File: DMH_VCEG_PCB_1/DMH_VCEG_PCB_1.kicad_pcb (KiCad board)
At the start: 2 copper layers, 148 x 175 mm, 243 parts, among them J1 TS_Jack_6.35mm_Sw, J10 TS_Jack_6.35mm_Sw, J100 IDC_02x08, J11 TS_Jack_6.35mm_Sw, J12 TS_Jack_6.35mm_Sw, J13 TS_Jack_6.35mm_Sw, J14 TS_Jack_6.35mm_Sw, J15 TS_Jack_6.35mm_Sw, J16 TS_Jack_6.35mm_Sw, J17 TS_Jack_6.35mm_Sw, J18 TS_Jack_6.35mm_Sw, J19 TS_Jack_6.35mm_Sw, J2 TS_Jack_6.35mm_Sw, J20 TS_Jack_6.35mm_Sw, J200 IDC_02x08, J21 Conn_01x10_PinHeader, J22 Conn_01x10_PinHeader, J23 Conn_01x10_PinHeader, J24 Conn_01x06_PinHeader, J25 Conn_01x10_PinHeader, J26 Conn_01x10_PinHeader, J27 Conn_01x10_PinHeader, J3 TS_Jack_6.35mm_Sw, J4 TS_Jack_6.35mm_Sw, J5 TS_Jack_6.35mm_Sw, J6 TS_Jack_6.35mm_Sw, J7 TS_Jack_6.35mm_Sw, J8 TS_Jack_6.35mm_Sw, J9 TS_Jack_6.35mm_Sw, Q1 BC558, Q17 BC558, Q18 BC558, Q19 BC548, Q2 BC558, Q20 BC548, Q21 BS170, Q22 BS170, Q3 BC548, Q4 BC548, Q5 BS170, Q6 BS170, U1 TL074, U11 TL074, U12 4001, U13 40106, U15 TL074, U16 4001, U17 TL074, U2 4001, U25 4001, U3 40106, U5 TL074, U6 4001, U7 TL074

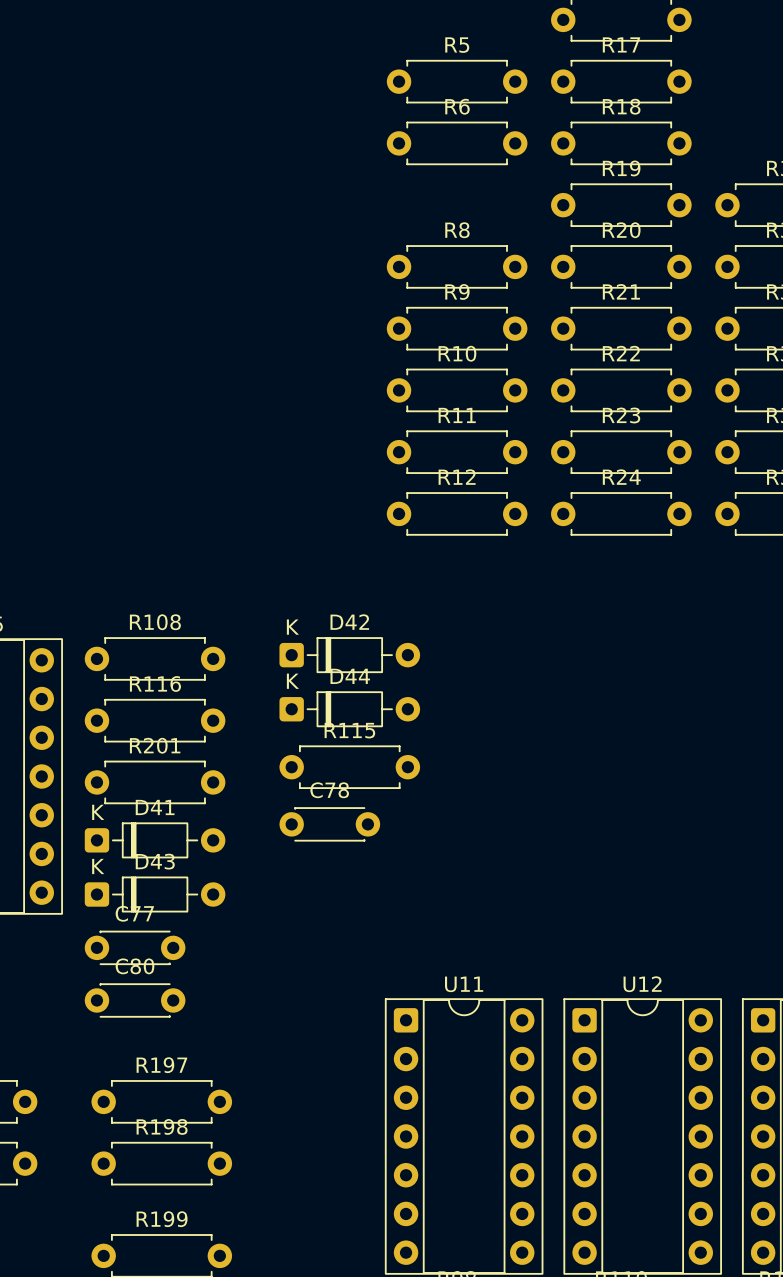
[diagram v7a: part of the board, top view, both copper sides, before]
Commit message: Synced PCB 2 schematic to PCB 1
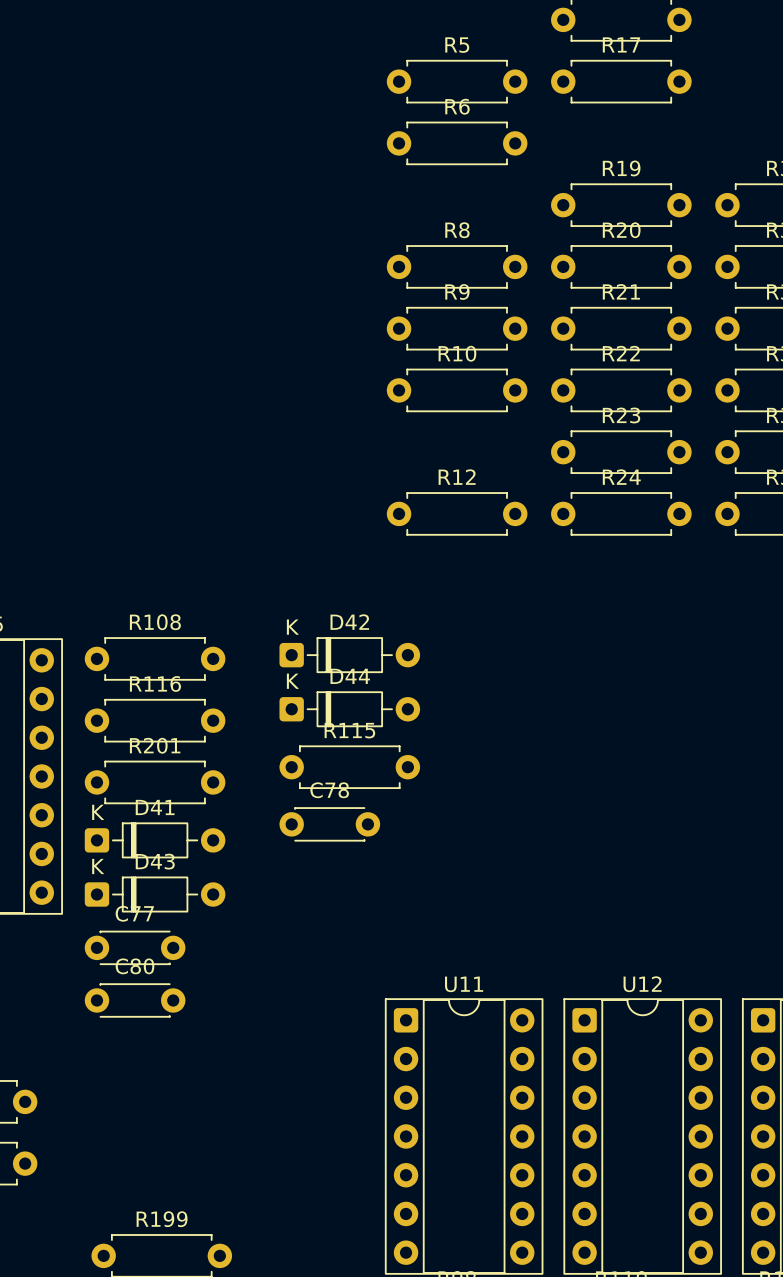
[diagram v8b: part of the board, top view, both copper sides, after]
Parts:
- removed R11, R198: 100k, Resistor_THT:R_Axial_DIN0207_L6.3mm_D2.5mm_P7.62mm_Horizontal
- removed R18, R197: 68k, Resistor_THT:R_Axial_DIN0207_L6.3mm_D2.5mm_P7.62mm_Horizontal
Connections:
- J1 pad T: Net-(J23D-Pin_4) -> Net-(J22B-Pin_2)
- J11 pad T: Net-(J27D-Pin_4) -> Net-(J26B-Pin_2)
- J12 pad T: Net-(J27E-Pin_5) -> Net-(J26D-Pin_4)
- J13 pad T: Net-(J27H-Pin_8) -> Net-(J27C-Pin_3)
- J14 pad T: Net-(J27I-Pin_9) -> Net-(J27H-Pin_8)
- J2 pad T: Net-(J23E-Pin_5) -> Net-(J22D-Pin_4)
- J21 pad 2: /Core Circuit A/Dec_State -> /CV Processing A/Sus CV
- J21 pad 3: /Core Circuit A/Sus_State -> /CV Processing A/Att CV
- J21 pad 4: /Core Circuit A/Att_State -> /Core Circuit A/Dec_State
- J21 pad 5: /Core Circuit A/Rel_State -> /Core Circuit A/Sus_State
- J21 pad 7: Net-(J21G-Pin_7) -> /CV Processing A/Max Level
- J21 pad 8: /Core Circuit A/Out -> /Core Circuit A/Att_State
- J21 pad 9: Net-(J21I-Pin_9) -> /Core Circuit A/Rel_State
- J22 pad 2: /Core Circuit A/Inv Sus State -> Net-(J22B-Pin_2)
- J22 pad 4: /CV Processing A/Max Level -> Net-(J22D-Pin_4)
- J22 pad 5: /CV Processing A/Att CV -> /Core Circuit A/Inv Sus State
- J22 pad 6: /CV Processing A/Dec CV -> /Core Circuit A/Out
- J22 pad 7: /CV Processing A/Sus CV -> /CV Processing A/Dec CV
- J23 pad 10: unconnected-(J23J-Pin_10-Pad10) -> Net-(J23J-Pin_10)
- J23 pad 3: unconnected-(J23C-Pin_3-Pad3) -> Net-(J23C-Pin_3)
- J23 pad 4: Net-(J23D-Pin_4) -> unconnected-(J23D-Pin_4-Pad4)
- J23 pad 5: Net-(J23E-Pin_5) -> unconnected-(J23E-Pin_5-Pad5)
- J24 pad 2: Net-(J24B-Pin_2) -> /Core Circuit A/ProcGate
- J24 pad 3: /Core Circuit A/ProcGate -> Net-(J24C-Pin_3)
- J25 pad 2: /Core Circuit B/Dec_State -> /CV Processing B/Sus CV
- J25 pad 3: /Core Circuit B/Sus_State -> /CV Processing B/Att CV
- J25 pad 4: /Core Circuit B/Att_State -> /Core Circuit B/Sus_State
- J25 pad 5: /Core Circuit B/Rel_State -> /Core Circuit B/Dec_State
- J25 pad 6: Net-(J25F-Pin_6) -> /CV Processing B/Max Level
- J25 pad 7: Net-(J25G-Pin_7) -> /Core Circuit B/Rel_State
- J25 pad 8: /Core Circuit B/Out -> /Core Circuit B/Att_State
- J26 pad 2: /Core Circuit B/Inv Sus State -> Net-(J26B-Pin_2)
- J26 pad 4: /CV Processing B/Max Level -> Net-(J26D-Pin_4)
- J26 pad 5: /CV Processing B/Att CV -> /Core Circuit B/Inv Sus State
- J26 pad 7: /CV Processing B/Sus CV -> /Core Circuit B/Out
- J27 pad 10: unconnected-(J27J-Pin_10-Pad10) -> Net-(J27J-Pin_10)
- J27 pad 3: unconnected-(J27C-Pin_3-Pad3) -> Net-(J27C-Pin_3)
- J27 pad 4: Net-(J27D-Pin_4) -> unconnected-(J27D-Pin_4-Pad4)
- J27 pad 5: Net-(J27E-Pin_5) -> unconnected-(J27E-Pin_5-Pad5)
- J3 pad T: Net-(J23H-Pin_8) -> Net-(J23C-Pin_3)
- J4 pad T: Net-(J23I-Pin_9) -> Net-(J23H-Pin_8)
- Q21 pad 1: Net-(J25F-Pin_6) -> Net-(J27J-Pin_10)
- Q22 pad 1: Net-(J25F-Pin_6) -> Net-(J27J-Pin_10)
- Q5 pad 1: Net-(J21F-Pin_6) -> Net-(J23J-Pin_10)
- Q6 pad 1: Net-(J21F-Pin_6) -> Net-(J23J-Pin_10)
- R104 pad 1: Net-(J25I-Pin_9) -> Net-(J27I-Pin_9)
- R7 pad 1: Net-(J21I-Pin_9) -> Net-(J23I-Pin_9)
- U15 pad 5: Net-(J25G-Pin_7) -> Net-(J25I-Pin_9)
- U17 pad 10: Net-(J25F-Pin_6) -> Net-(J27J-Pin_10)
- U25 pad 3: Net-(J24B-Pin_2) -> Net-(J24C-Pin_3)
- U25 pad 5: Net-(J24B-Pin_2) -> Net-(J24C-Pin_3)
- U5 pad 5: Net-(J21G-Pin_7) -> Net-(J21F-Pin_6)
- U7 pad 10: Net-(J21F-Pin_6) -> Net-(J23J-Pin_10)
